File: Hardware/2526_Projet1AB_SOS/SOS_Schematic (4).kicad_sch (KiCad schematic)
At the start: 42 parts, among them J1 USB_B_Mini, J2 Conn_02x10_Odd_Even, J3 Conn_01x02, SW1 SW_SPDT, U1 BU33SD5WG-TR, U2 STM32L476RGTx, U3 HTRC11001T, Y1 13,56MHz, Y2 8MHz

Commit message: BOM
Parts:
- H1, H2, H3, H4: now in the parts list

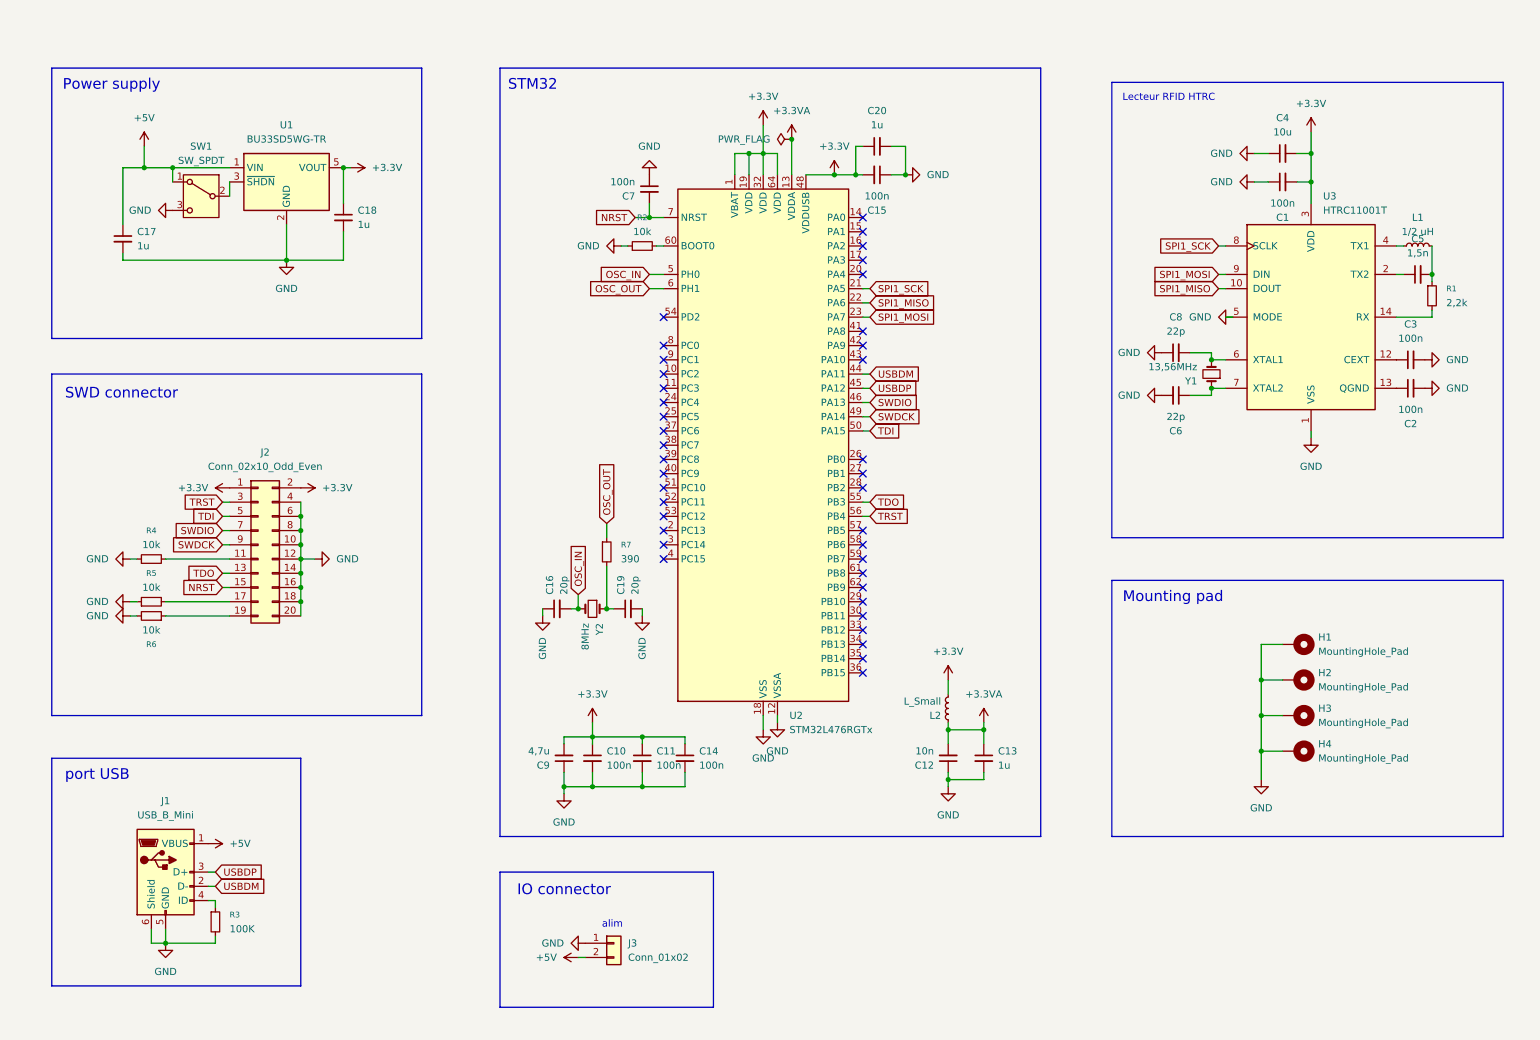
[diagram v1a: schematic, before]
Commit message: Update KiCAD Schematic: SWD
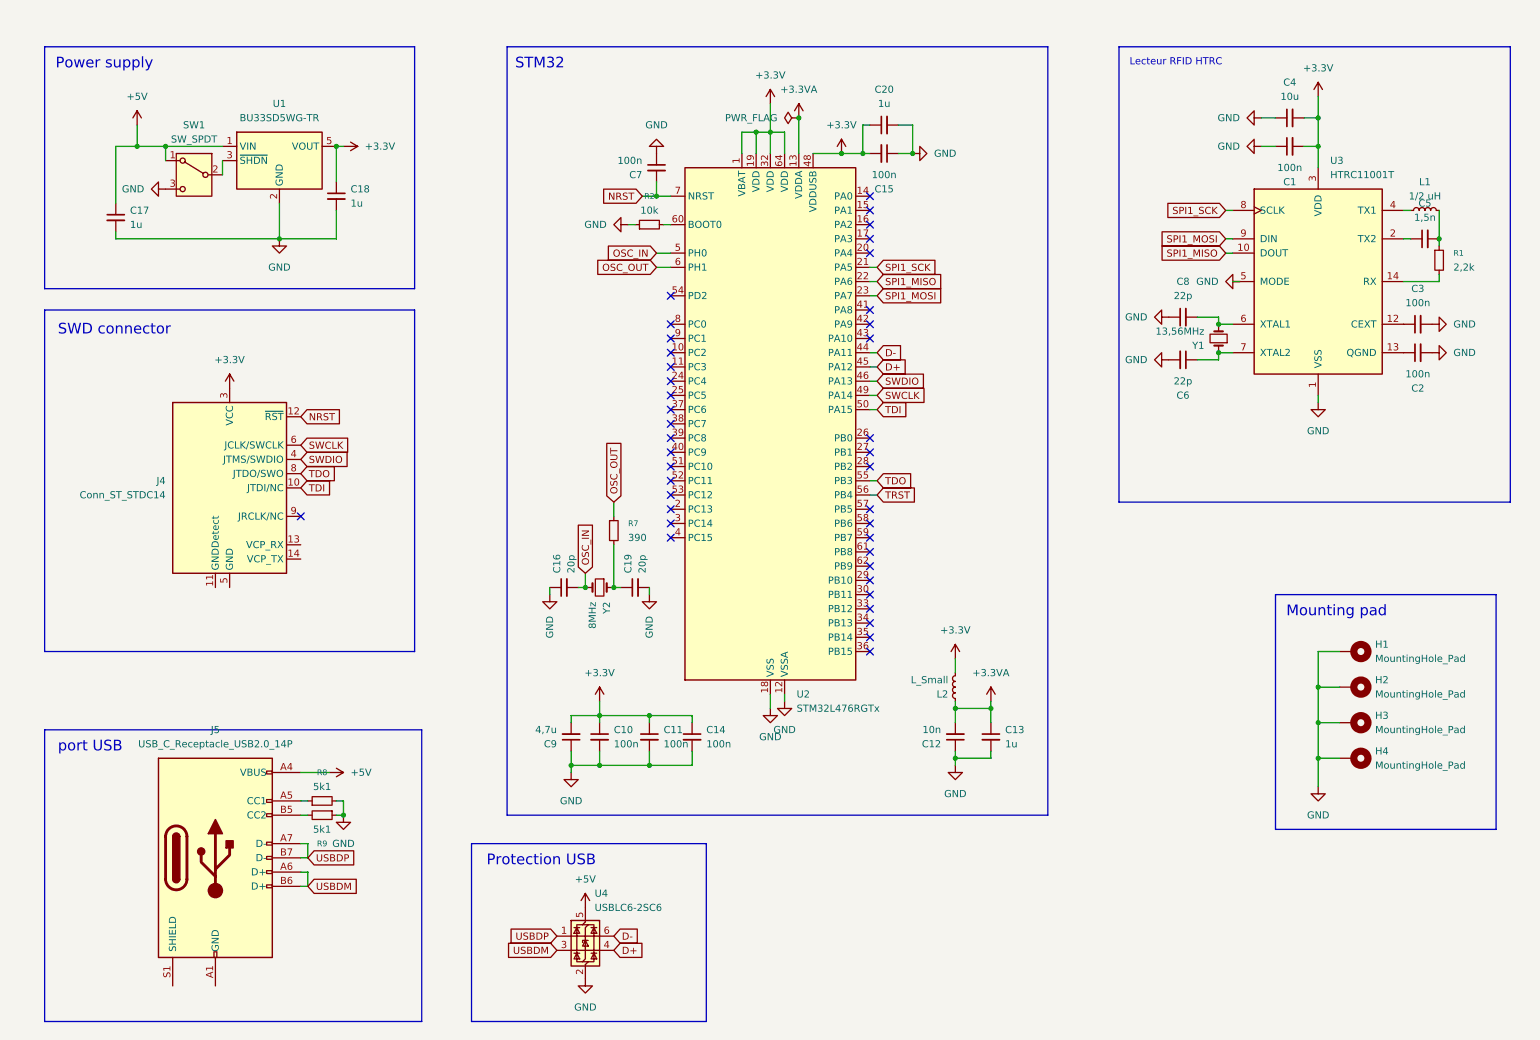
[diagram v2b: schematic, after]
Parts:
- removed J1: USB_B_Mini, Connector_USB:USB_Mini-B_Tensility_54-00023_Vertical, symbol Connector:USB_B_Mini
- removed J2: Conn_02x10_Odd_Even, Connector_PinHeader_1.27mm:PinHeader_2x10_P1.27mm_Vertical_SMD, symbol Connector_Generic:Conn_02x10_Odd_Even
- removed J3: Conn_01x02, Connector_JST:JST_XH_B2B-XH-A_1x02_P2.50mm_Vertical, symbol Connector_Generic:Conn_01x02
- removed R3: 100K, Resistor_SMD:R_0805_2012Metric_Pad1.20x1.40mm_HandSolder, symbol Device:R_Small
- removed R4, R5, R6: 10k, Resistor_SMD:R_0805_2012Metric_Pad1.20x1.40mm_HandSolder, symbol Device:R_Small
- added J4: Conn_ST_STDC14, symbol Connector:Conn_ST_STDC14
- added J5: USB_C_Receptacle_USB2.0_14P, symbol Connector:USB_C_Receptacle_USB2.0_14P
- added R8, R9: 5k1, symbol Device:R_Small
- added U4: USBLC6-2SC6, Package_TO_SOT_SMD:SOT-23-6, symbol Power_Protection:USBLC6-2SC6
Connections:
- net +3.3V: now also J4.3 (VCC)
- net +5V: now also J5.A4 (VBUS), J5.A9 (VBUS), J5.B4 (VBUS), J5.B9 (VBUS), U4.5 (VBUS)
- net GND: now also R8.2, R9.1, U4.2 (GND)
- net NRST: now also J4.12 (~{RST})
- net SWDIO: now also J4.4 (JTMS/SWDIO)
- net TDI: now also J4.10 (JTDI/NC)
- net TDO: now also J4.8 (JTDO/SWO)
- net USBDM: now also J5.A6 (D+), J5.B6 (D+), U4.3 (I/O2); no longer U2.44 (PA11)
- net USBDP: now also J5.A7 (D-), J5.B7 (D-), U4.1 (I/O1); no longer U2.45 (PA12)
- net SWDCK renamed SWCLK
- net SWCLK: now also J4.6 (JCLK/SWCLK)
- new net: J4.5 (GND), J4.7 (GND)
- new net: J5.B5 (CC2), R9.2
- new net: J5.A5 (CC1), R8.1
- new net: J5.A1 (GND), J5.A12 (GND), J5.B1 (GND), J5.B12 (GND)
- new net D+: U2.45 (PA12), U4.4 (I/O2)
- new net D-: U2.44 (PA11), U4.6 (I/O1)
- no-connect marks 39 -> 40
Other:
- note added: "Protection USB"
- note removed: "IO connector"
- note removed: "alim"
- moved on the sheet: C1, C10, C11, C12, C13, C14, C15, C16, C17, C18, C19, C2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

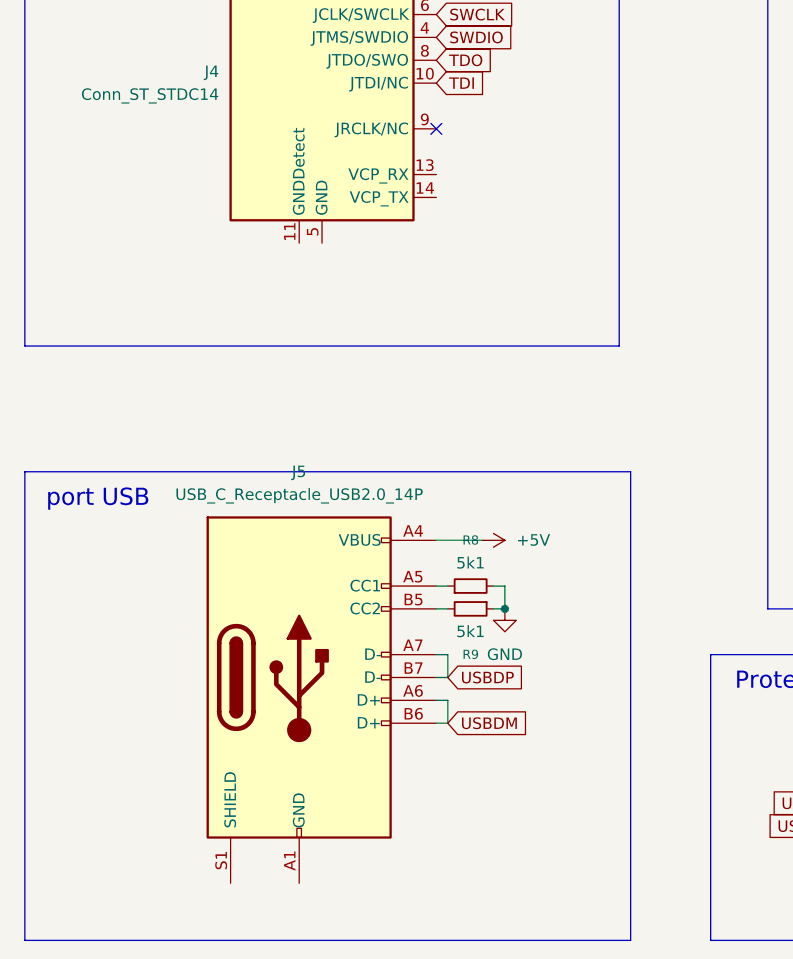
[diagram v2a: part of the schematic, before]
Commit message: Update schematic: RFID left
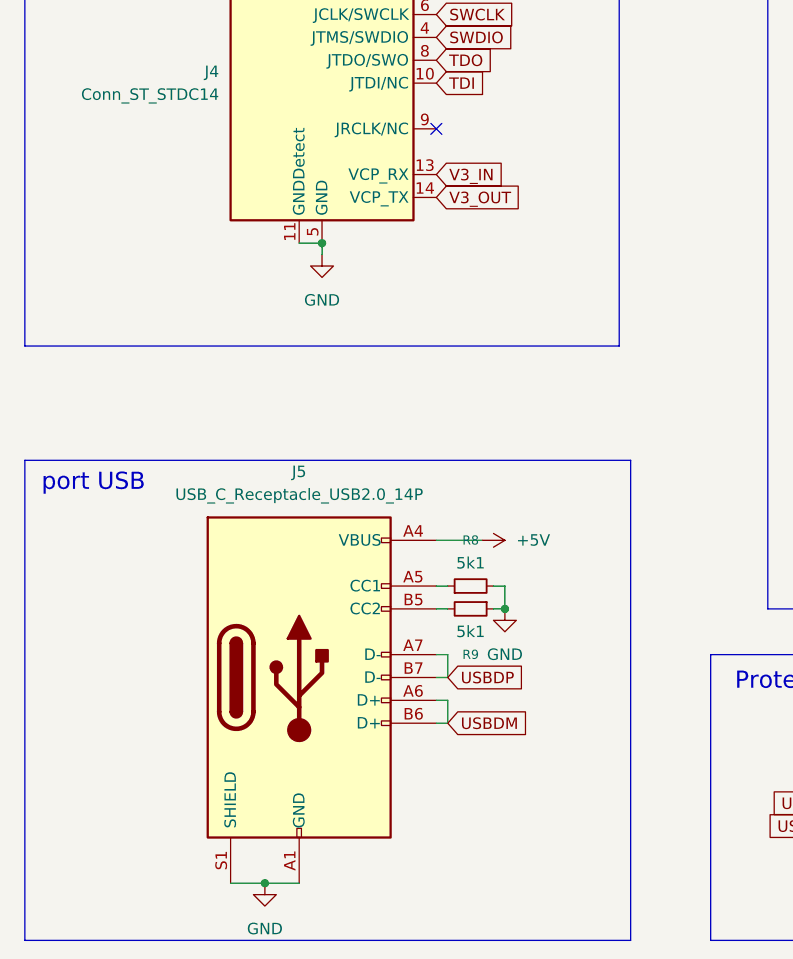
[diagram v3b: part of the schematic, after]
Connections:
- net GND: now also J4.11 (GNDDetect), J4.5 (GND), J4.7 (GND), J5.A1 (GND), J5.A12 (GND), J5.B1 (GND), J5.B12 (GND), J5.S1 (SHIELD)
- net V3_IN: now reaches J4.13 (VCP_RX)
- net V3_OUT: now reaches J4.14 (VCP_TX)
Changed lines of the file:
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@@
 	)
 	(rectangle
-		(start 19.05 142.24)
+		(start 19.05 140.97)
 		(end 86.36 194.31)
 		(stroke
@@
 	(text "port USB"
 		(exclude_from_sim no)
-		(at 27.178 145.288 0)
+		(at 26.67 143.51 0)
 		(effects
 			(font
@@
 	)
 	(junction
+		(at 45.72 187.96)
+		(diameter 0)
+		(color 0 0 0 0)
+	)
+	(junction
 		(at 246.38 147.32)
 		(diameter 0)
@@
 	)
 	(junction
+		(at 52.07 116.84)
+		(diameter 0)
+		(color 0 0 0 0)
+	)
+	(junction
 		(at 187.96 138.43)
 		(diameter 0)
@@
 	(wire
 		(pts
+			(xy 52.07 116.84) (xy 52.07 118.11)
+		)
+		(stroke
+			(width 0)
+			(type default)
+		)
+	)
+	(wire
+		(pts
 			(xy 166.37 64.77) (xy 167.64 64.77)
 		)
@@
 	(wire
 		(pts
+			(xy 49.53 116.84) (xy 52.07 116.84)
+		)
+		(stroke
+			(width 0)
+			(type default)
+		)
+	)
+	(wire
+		(pts
 			(xy 118.11 148.59) (xy 127 148.59)
 		)
@@
 	(wire
 		(pts
+			(xy 41.91 187.96) (xy 45.72 187.96)
+		)
+		(stroke
+			(width 0)
+			(type default)
+		)
+	)
+	(wire
+		(pts
 			(xy 166.37 59.69) (xy 167.64 59.69)
 		)
@@
 	(wire
 		(pts
+			(xy 45.72 187.96) (xy 49.53 187.96)
+		)
+		(stroke
+			(width 0)
+			(type default)
+		)
+	)
+	(wire
+		(pts
 			(xy 181.61 146.05) (xy 181.61 147.32)
 		)
@@
 		)
 	)
+	(global_label "V3_OUT"
+		(shape input)
+		(at 64.77 111.76 0)
+		(fields_autoplaced yes)
+		(effects
+			(font
+				(size 1.27 1.27)
+			)
+			(justify left)
+		)
+		(property "Intersheetrefs" "${INTERSHEET_REFS}"
+			(at 74.6495 111.76 0)
+			(effects
+				(font
+					(size 1.27 1.27)
+				)
+				(justify left)
+				(hide yes)
+			)
+		)
+	)
 	(global_label "USBDM"
 		(shape input)
@@
 		)
 	)
+	(global_label "V3_IN"
+		(shape input)
+		(at 64.77 109.22 0)
+		(fields_autoplaced yes)
+		(effects
+			(font
+				(size 1.27 1.27)
+			)
+			(justify left)
+		)
+		(property "Intersheetrefs" "${INTERSHEET_REFS}"
+			(at 72.9562 109.22 0)
+			(effects
+				(font
+					(size 1.27 1.27)
+				)
+				(justify left)
+				(hide yes)
+			)
+		)
+	)
 	(global_label "OSC_IN"
 		(shape input)
@@
 	)
 	(symbol
+		(lib_id "power:GND")
+		(at 52.07 118.11 0)
+		(unit 1)
+		(exclude_from_sim no)
+		(in_bom yes)
+		(on_board yes)
+		(dnp no)
+		(fields_autoplaced yes)
+		(property "Reference" "#PWR029"
+			(at 52.07 124.46 0)
+			(effects
+				(font
+					(size 1.27 1.27)
+				)
+				(hide yes)
+			)
+		)
+		(property "Value" "GND"
+			(at 52.07 123.19 0)
+			(effects
+				(font
+					(size 1.27 1.27)
+				)
+			)
+		)
+		(property "Footprint" ""
+			(at 52.07 118.11 0)
+			(effects
+				(font
+					(size 1.27 1.27)
+				)
+				(hide yes)
+			)
+		)
+		(property "Datasheet" ""
+			(at 52.07 118.11 0)
+			(effects
+				(font
+					(size 1.27 1.27)
+				)
+				(hide yes)
+			)
+		)
+		(property "Description" "Power symbol creates a global label with name \"GND\" , ground"
+			(at 52.07 118.11 0)
+			(effects
+				(font
+					(size 1.27 1.27)
+				)
+				(hide yes)
+			)
+		)
+		(pin "1"
+		)
+		(instances
+			(project ""
+				(path "/9d394b3d-e5c0-4919-a596-896a666dc5cf"
+					(reference "#PWR029")
+					(unit 1)
+				)
+			)
+		)
+	)
+	(symbol
 		(lib_id "Device:Crystal_Small")
 		(at 228.6 72.39 90)
@@
 					(unit 1)
 				)
+			)
+		)
+	)
+	(symbol
+		(lib_id "power:GND")
+		(at 45.72 187.96 0)
+		(unit 1)
+		(exclude_from_sim no)
+		(in_bom yes)
+		(on_board yes)
+		(dnp no)
+		(fields_autoplaced yes)
+		(property "Reference" "#PWR030"
+			(at 45.72 194.31 0)
+			(effects
+				(font
+					(size 1.27 1.27)
+				)
+				(hide yes)
+			)
+		)
+		(property "Value" "GND"
+			(at 45.72 193.04 0)
+			(effects
+				(font
+					(size 1.27 1.27)
+				)
+			)
+		)
+		(property "Footprint" ""
+			(at 45.72 187.96 0)
+			(effects
+				(font
+					(size 1.27 1.27)
+				)
+				(hide yes)
+			)
+		)
+		(property "Datasheet" ""
+			(at 45.72 187.96 0)
+			(effects
+				(font
+					(size 1.27 1.27)
+				)
+				(hide yes)
+			)
+		)
+		(property "Description" "Power symbol creates a global label with name \"GND\" , ground"
+			(at 45.72 187.96 0)
+			(effects
+				(font
+					(size 1.27 1.27)
+				)
+				(hide yes)
+			)
+		)
+		(pin "1"
+		)
+		(instances
+			(project ""
+				(path "/9d394b3d-e5c0-4919-a596-896a666dc5cf"
+					(reference "#PWR030")
+					(unit 1)
+				)

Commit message: work on schematic and updating board
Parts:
- R8, R9: footprint (none) -> Resistor_SMD:R_0805_2012Metric_Pad1.20x1.40mm_HandSolder
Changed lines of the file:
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@@
 	)
 	(junction
+		(at 35.56 35.56)
+		(diameter 0)
+		(color 0 0 0 0)
+	)
+	(junction
 		(at 181.61 138.43)
 		(diameter 0)
@@
 	(wire
 		(pts
+			(xy 35.56 35.56) (xy 35.56 38.1)
+		)
+		(stroke
+			(width 0)
+			(type default)
+		)
+	)
+	(wire
+		(pts
 			(xy 118.11 148.59) (xy 127 148.59)
 		)
@@
 	(wire
 		(pts
-			(xy 35.56 34.29) (xy 35.56 38.1)
+			(xy 35.56 34.29) (xy 35.56 35.56)
 		)
 		(stroke
@@
 	)
 	(symbol
+		(lib_id "power:PWR_FLAG")
+		(at 35.56 35.56 90)
+		(unit 1)
+		(exclude_from_sim no)
+		(in_bom yes)
+		(on_board yes)
+		(dnp no)
+		(fields_autoplaced yes)
+		(property "Reference" "#FLG02"
+			(at 33.655 35.56 0)
+			(effects
+				(font
+					(size 1.27 1.27)
+				)
+				(hide yes)
+			)
+		)
+		(property "Value" "PWR_FLAG"
+			(at 31.75 35.5599 90)
+			(effects
+				(font
+					(size 1.27 1.27)
+				)
+				(justify left)
+			)
+		)
+		(property "Footprint" ""
+			(at 35.56 35.56 0)
+			(effects
+				(font
+					(size 1.27 1.27)
+				)
+				(hide yes)
+			)
+		)
+		(property "Datasheet" "~"
+			(at 35.56 35.56 0)
+			(effects
+				(font
+					(size 1.27 1.27)
+				)
+				(hide yes)
+			)
+		)
+		(property "Description" "Special symbol for telling ERC where power comes from"
+			(at 35.56 35.56 0)
+			(effects
+				(font
+					(size 1.27 1.27)
+				)
+				(hide yes)
+			)
+		)
+		(pin "1"
+		)
+		(instances
+			(project ""
+				(path "/9d394b3d-e5c0-4919-a596-896a666dc5cf"
+					(reference "#FLG02")
+					(unit 1)
+				)
+			)
+		)
+	)
+	(symbol
 		(lib_id "power:GND")
 		(at 148.59 138.43 0)
@@
 			)
 		)
-		(property "Footprint" ""
+		(property "Footprint" "Resistor_SMD:R_0805_2012Metric_Pad1.20x1.40mm_HandSolder"
 			(at 68.58 157.48 0)
 			(effects
@@
 			)
 		)
-		(property "Footprint" ""
+		(property "Footprint" "Resistor_SMD:R_0805_2012Metric_Pad1.20x1.40mm_HandSolder"
 			(at 68.58 154.94 0)
 			(effects
